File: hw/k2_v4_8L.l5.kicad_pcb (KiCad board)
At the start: 8 copper layers, 120 x 46 mm, 59 parts, among them J11 J_EC_HEADER, J12 J_12V_IN, J13 J_SWD, J2 SlimSAS_x8_SFF8654, J3 MCIO_4i_SFF1016, J4 MCIO_4i_SFF1016, J6 J_PWR_CTRL, J9 J_OOB_HEADER, U1 STM32G0B1CBT6, U2 DCDC_12V_3V3, U4 BAT54C, U5 OPTO_LTV356T, U6 DS320PR1601

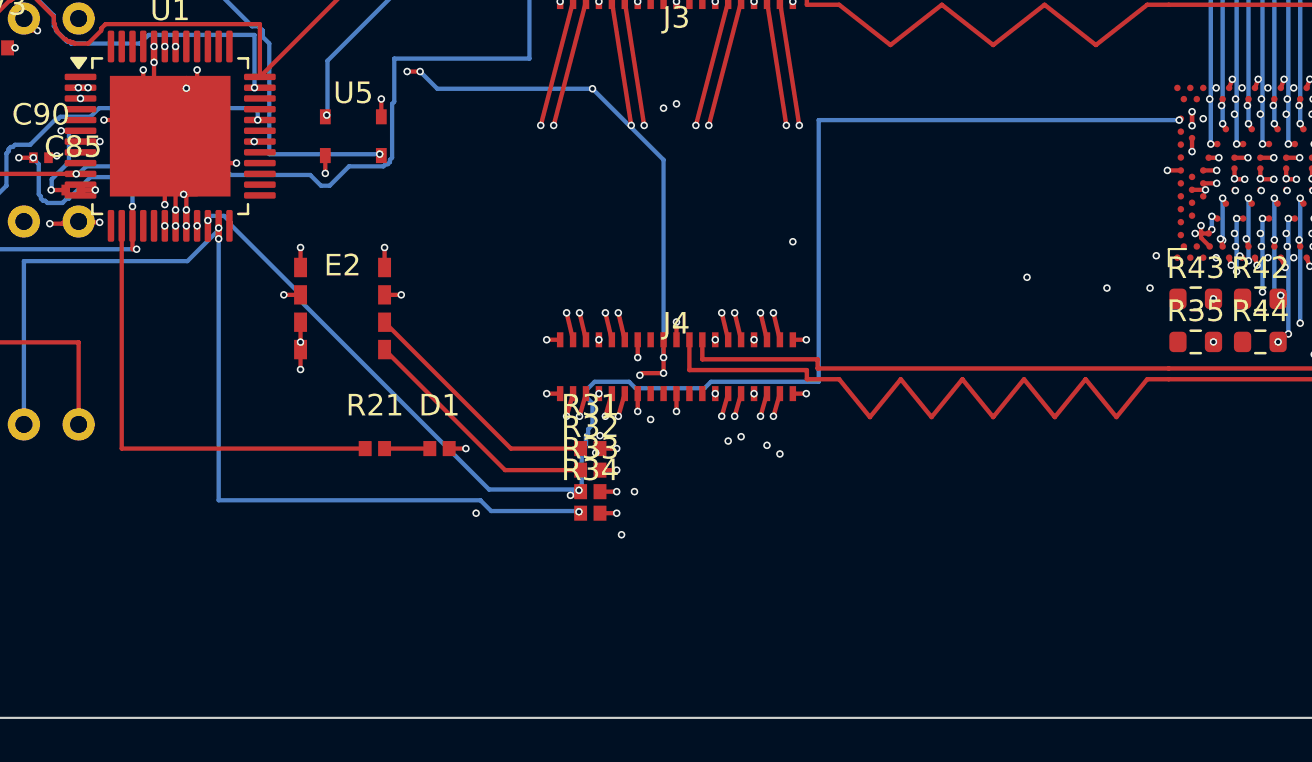
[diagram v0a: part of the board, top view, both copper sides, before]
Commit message: p4(k2): 收敛增量 7（L2 自裁）—— 跨层布线搜索加强（阶段 F3 修订）+ T-8 测量陷阱登记
- F3 修订：过孔搜索半径 1.5->2.5mm、角步 15->10 度；每端锚点 3->8；收尾连接器补 45+轴两段变体（口径/精确复核放行闸不变）。
- 实测：未连接 31 -> 29（+2 条）；违规 75 -> 75（类型集不变）；判定器 PASS5/FAIL5 集合未变；非 45 度 2051 未增。
- T-8（测量陷阱）：以无同名 .kicad_pro 的中间件为输入时，输出件缺 pro => kicad-cli drc 回退 KiCad 默认规则
  （min via 0.5 / track 0.2 / drill 0.3 / 板边 0.5），把板内既有 0.20/0.35 过孔与 0.16 PCIe 走线全判违规
  （本轮实测假象 1020 条）=> DRC 结论一律取「仓库路径 + 同名 pro」口径。
- 结构性结论：剩余 29 条 = no-legal-via-slot 14（U6 BGA 格内球无 F.Cu 逃逸通道）+ no-legal-path-on-bcu 15（J2 长距离段）
  => 续做须重解 U6 逃逸走廊（走廊 = L2，可自裁）或请监理裁定口径。
- 边界：未动 l4/设计源板/真源 yaml/criteria/SPEC rev-19..34 原件；未派 WORKER；临时仅 /tmp/opencode。
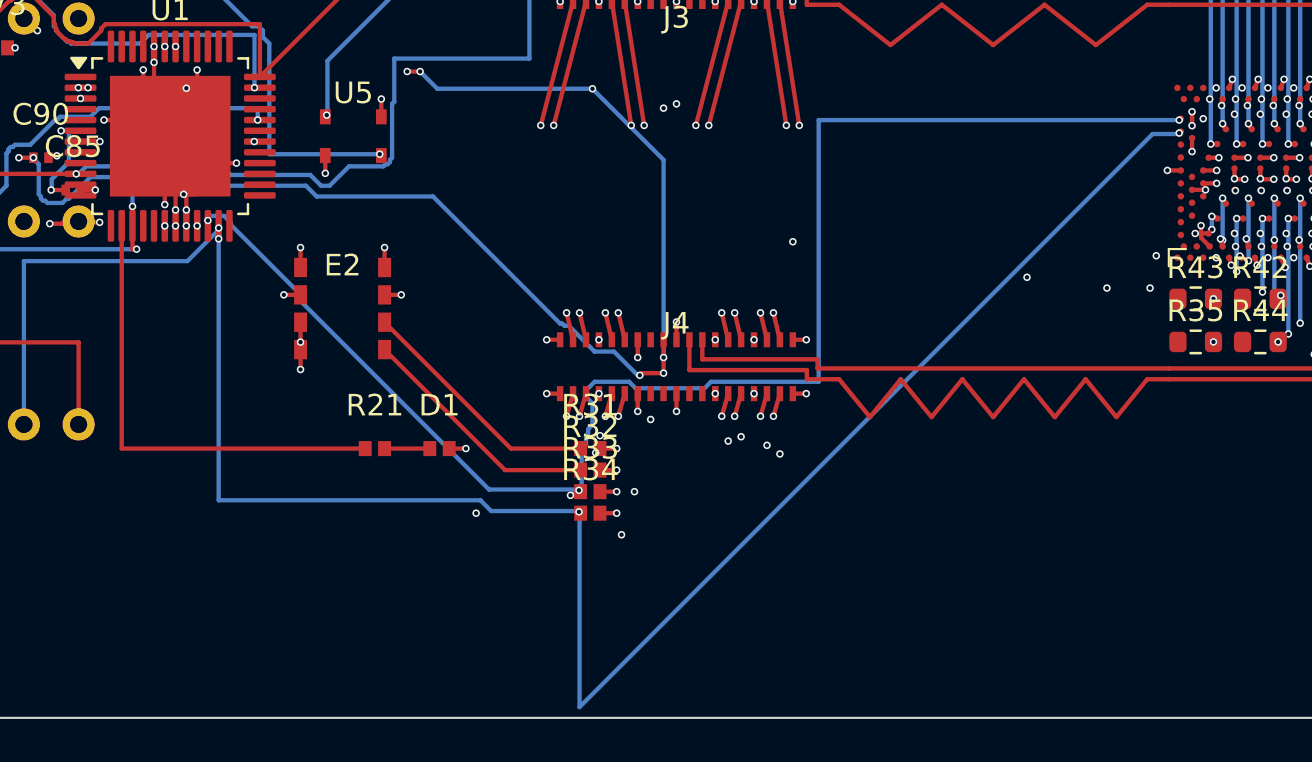
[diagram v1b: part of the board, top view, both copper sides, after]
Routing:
- net I2C2_SDA: track 47.2 -> 95.2 mm, vias 3 -> 4
- net P3V3_AUX: track 58.7 -> 86.1 mm
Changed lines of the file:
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@@
 	)
 	(segment
+		(start 42.3 54.3)
+		(end 42.8 54.8)
+		(width 0.2)
+		(layer "B.Cu")
+		(net "P3V3_AUX")
+	)
+	(segment
 		(start 58.9 53.1)
 		(end 58.9 62.275)
@@
 	)
 	(segment
+		(start 57.7 63.1)
+		(end 57.8 63.1)
+		(width 0.2)
+		(layer "B.Cu")
+		(net "P3V3_AUX")
+	)
+	(segment
+		(start 38.6 54.3)
+		(end 42.3 54.3)
+		(width 0.2)
+		(layer "B.Cu")
+		(net "P3V3_AUX")
+	)
+	(segment
 		(start 30.1 55)
 		(end 30.2 55)
@@
 	)
 	(segment
+		(start 34.2 53.9)
+		(end 38.2 53.9)
+		(width 0.2)
+		(layer "B.Cu")
+		(net "P3V3_AUX")
+	)
+	(segment
 		(start 26.5 57.2458)
 		(end 34.441 57.2458)
@@
 	)
 	(segment
+		(start 48.2 54.8)
+		(end 54.1 60.7)
+		(width 0.2)
+		(layer "B.Cu")
+		(net "P3V3_AUX")
+	)
+	(segment
+		(start 38.2 53.9)
+		(end 38.6 54.3)
+		(width 0.2)
+		(layer "B.Cu")
+		(net "P3V3_AUX")
+	)
+	(segment
 		(start 30.2 55)
 		(end 30.3 55.1)
@@
 	)
 	(segment
+		(start 54.5 60.8)
+		(end 55.7 62)
+		(width 0.2)
+		(layer "B.Cu")
+		(net "P3V3_AUX")
+	)
+	(segment
+		(start 54.1 60.7)
+		(end 54.2 60.7)
+		(width 0.2)
+		(layer "B.Cu")
+		(net "P3V3_AUX")
+	)
+	(segment
+		(start 42.8 54.8)
+		(end 48.2 54.8)
+		(width 0.2)
+		(layer "B.Cu")
+		(net "P3V3_AUX")
+	)
+	(segment
+		(start 54.3 60.8)
+		(end 54.5 60.8)
+		(width 0.2)
+		(layer "B.Cu")
+		(net "P3V3_AUX")
+	)
+	(segment
+		(start 54.2 60.7)
+		(end 54.3 60.8)
+		(width 0.2)
+		(layer "B.Cu")
+		(net "P3V3_AUX")
+	)
+	(segment
 		(start 29.9 54.7)
 		(end 30 54.8)
@@
 	)
 	(segment
+		(start 56.6 62)
+		(end 57.7 63.1)
+		(width 0.2)
+		(layer "B.Cu")
+		(net "P3V3_AUX")
+	)
+	(segment
 		(start 30 54.8)
 		(end 30 54.9)
@@
 	)
 	(segment
+		(start 55.7 62)
+		(end 56.6 62)
+		(width 0.2)
+		(layer "B.Cu")
+		(net "P3V3_AUX")
+	)
+	(segment
 		(start 47.6 49)
 		(end 48.4 49.8)
@@
 	)
 	(segment
+		(start 82.91 51.79)
+		(end 82.8334 51.79)
+		(width 0.2)
+		(layer "F.Cu")
+		(net "I2C2_SDA")
+	)
+	(segment
 		(start 38.25 56.1625)
 		(end 38.25 56.7625)
@@
 		(net "I2C2_SDA")
 	)
+	(segment
+		(start 82.8334 51.79)
+		(end 82.8334 51.8543)
+		(width 0.2)
+		(layer "F.Cu")
+		(net "I2C2_SDA")
+	)
+	(via
+		(at 82.8334 51.8543)
+		(size 0.35)
+		(drill 0.2)
+		(layers "F.Cu" "B.Cu")
+		(net "I2C2_SDA")
+	)
 	(via
 		(at 38.25 56.7625)
@@
 	)
 	(segment
+		(start 82.8 51.9)
+		(end 81.6 51.9)
+		(width 0.2)
+		(layer "B.Cu")
+		(net "I2C2_SDA")
+	)
+	(segment
 		(start 38.25 68.9)
 		(end 38.25 56.7625)
 		(width 0.2)
 		(layer "B.Cu")
+		(net "I2C2_SDA")
+	)
+	(segment
+		(start 55 78.5)
+		(end 55 69.4)
+		(width 0.2)
+		(layer "B.Cu")
+		(net "I2C2_SDA")
+	)
+	(segment
+		(start 81.6 51.9)
+		(end 55 78.5)
+		(width 0.2)
+		(layer "B.Cu")

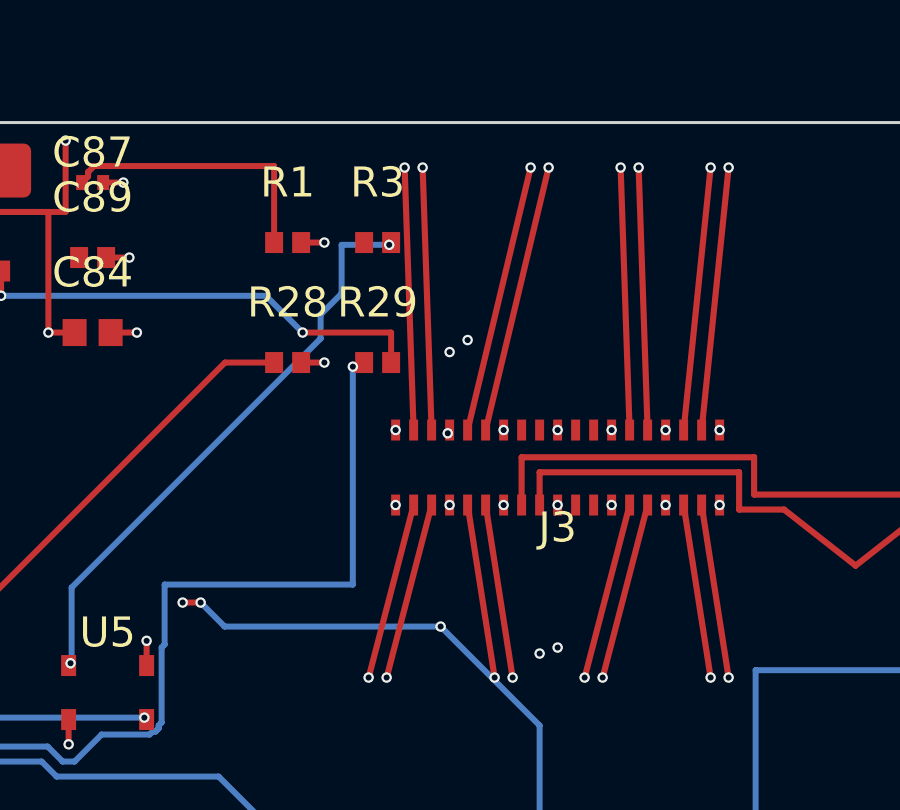
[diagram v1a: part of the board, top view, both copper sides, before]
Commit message: p4(k2): 收敛增量 8（L2 自裁）—— 阶段 F3 逃逸加强（盘中孔 VIP 兜底 + F.Cu A* 多腿逃逸）+ T-9/G-1 登记
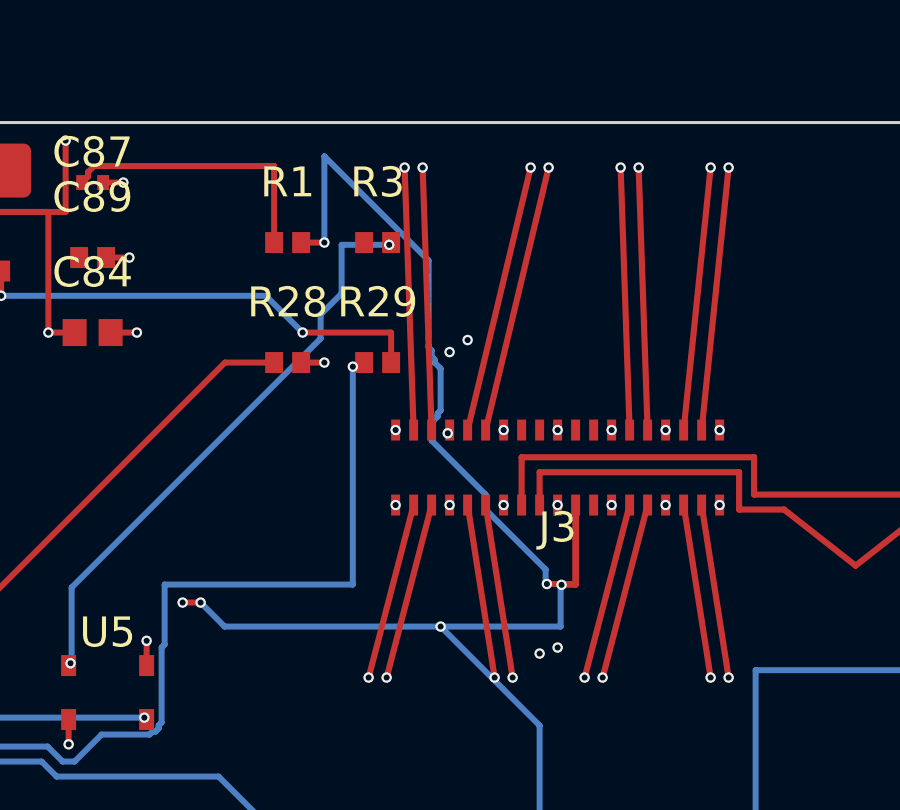
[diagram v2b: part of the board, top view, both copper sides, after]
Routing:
- net P3V3_AUX: track 86.1 -> 118.6 mm, vias 12 -> 14
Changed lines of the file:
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@@
+	)
+	(segment
+		(start 60.1 48.3811)
+		(end 59.1423 48.3811)
+		(width 0.2)
+		(layer "F.Cu")
+		(net "P3V3_AUX")
 	)
 	(segment
@@
 	)
 	(segment
+		(start 60.1 45.8)
+		(end 60.1 48.409)
+		(width 0.2)
+		(layer "F.Cu")
+		(net "P3V3_AUX")
+	)
+	(segment
 		(start 57.9 63)
 		(end 58.9 63)
@@
 	)
 	(segment
+		(start 60.1 45.8)
+		(end 60.1 48.3811)
+		(width 0.2)
+		(layer "F.Cu")
+		(net "P3V3_AUX")
+	)
+	(segment
+		(start 60.1 48.409)
+		(end 59.6311 48.409)
+		(width 0.2)
+		(layer "F.Cu")
+		(net "P3V3_AUX")
+	)
+	(segment
 		(start 31.75 61.57)
 		(end 31.75 65.38)
@@
 	)
 	(via
+		(at 59.6311 48.409)
+		(size 0.35)
+		(drill 0.2)
+		(layers "F.Cu" "B.Cu")
+		(net "P3V3_AUX")
+	)
+	(via
 		(at 26.5 61.57)
 		(size 0.35)
@@
 	(via
 		(at 47 49)
+		(size 0.35)
+		(drill 0.2)
+		(layers "F.Cu" "B.Cu")
+		(net "P3V3_AUX")
+	)
+	(via
+		(at 59.1423 48.3811)
 		(size 0.35)
 		(drill 0.2)
@@
 	)
 	(segment
+		(start 59.6 48.4)
+		(end 59.6 49.8)
+		(width 0.2)
+		(layer "B.Cu")
+		(net "P3V3_AUX")
+	)
+	(segment
 		(start 58.9 53.1)
 		(end 58.9 62.275)
@@
 	)
 	(segment
+		(start 55.2 40.5)
+		(end 55.2 37.6)
+		(width 0.2)
+		(layer "B.Cu")
+		(net "P3V3_AUX")
+	)
+	(segment
 		(start 30.3 55.1)
 		(end 31 55.1)
@@
 	)
 	(segment
+		(start 57.1 45.4)
+		(end 55.3 43.6)
+		(width 0.2)
+		(layer "B.Cu")
+		(net "P3V3_AUX")
+	)
+	(segment
+		(start 55.6 41.2)
+		(end 55.4 41)
+		(width 0.2)
+		(layer "B.Cu")
+		(net "P3V3_AUX")
+	)
+	(segment
+		(start 55.3 43)
+		(end 55.5 42.8)
+		(width 0.2)
+		(layer "B.Cu")
+		(net "P3V3_AUX")
+	)
+	(segment
+		(start 57.1 45.9)
+		(end 57.1 45.4)
+		(width 0.2)
+		(layer "B.Cu")
+		(net "P3V3_AUX")
+	)
+	(segment
 		(start 34.25 53.9)
 		(end 34.25 55.2625)
@@
 	)
 	(segment
+		(start 55.5 42.8)
+		(end 55.5 42.7)
+		(width 0.2)
+		(layer "B.Cu")
+		(net "P3V3_AUX")
+	)
+	(segment
 		(start 48.2 54.8)
 		(end 54.1 60.7)
@@
 	)
 	(segment
+		(start 55.4 41)
+		(end 55.4 40.9)
+		(width 0.2)
+		(layer "B.Cu")
+		(net "P3V3_AUX")
+	)
+	(segment
+		(start 55.2 37.6)
+		(end 51.725 34.125)
+		(width 0.2)
+		(layer "B.Cu")
+		(net "P3V3_AUX")
+	)
+	(segment
 		(start 30.2 55)
 		(end 30.3 55.1)
@@
 	)
 	(segment
+		(start 51.725 34.125)
+		(end 51.725 37)
+		(width 0.2)
+		(layer "B.Cu")
+		(net "P3V3_AUX")
+	)
+	(segment
 		(start 54.5 60.8)
 		(end 55.7 62)
@@
 	)
 	(segment
+		(start 59.1 48.4)
+		(end 59.1 47.9)
+		(width 0.2)
+		(layer "B.Cu")
+		(net "P3V3_AUX")
+	)
+	(segment
+		(start 55.4 40.9)
+		(end 55.3 40.8)
+		(width 0.2)
+		(layer "B.Cu")
+		(net "P3V3_AUX")
+	)
+	(segment
 		(start 54.3 60.8)
 		(end 54.5 60.8)
@@
 	)
 	(segment
+		(start 55.6 42.6)
+		(end 55.6 41.2)
+		(width 0.2)
+		(layer "B.Cu")
+		(net "P3V3_AUX")
+	)
+	(segment
 		(start 29.9 54.7)
 		(end 30 54.8)
@@
 	)
 	(segment
+		(start 55.3 40.6)
+		(end 55.2 40.5)
+		(width 0.2)
+		(layer "B.Cu")
+		(net "P3V3_AUX")
+	)
+	(segment
 		(start 56.6 62)
 		(end 57.7 63.1)
@@
 		(width 0.2)
 		(layer "B.Cu")
+		(net "P3V3_AUX")
+	)
+	(segment
+		(start 59.6 49.8)
+		(end 55.6 49.8)
+		(width 0.2)
+		(layer "B.Cu")
+		(net "P3V3_AUX")
+	)
+	(segment
+		(start 55.5 42.7)
+		(end 55.6 42.6)
+		(width 0.2)
+		(layer "B.Cu")
+		(net "P3V3_AUX")
+	)
+	(segment
+		(start 55.3 40.8)
+		(end 55.3 40.6)
+		(width 0.2)
+		(layer "B.Cu")
+		(net "P3V3_AUX")
+	)
+	(segment
+		(start 59.1 47.9)
+		(end 57.1 45.9)
+		(width 0.2)
+		(layer "B.Cu")
+		(net "P3V3_AUX")
+	)
+	(segment
+		(start 55.3 43.6)
+		(end 55.3 43)
+		(width 0.2)
+		(layer "B.Cu")

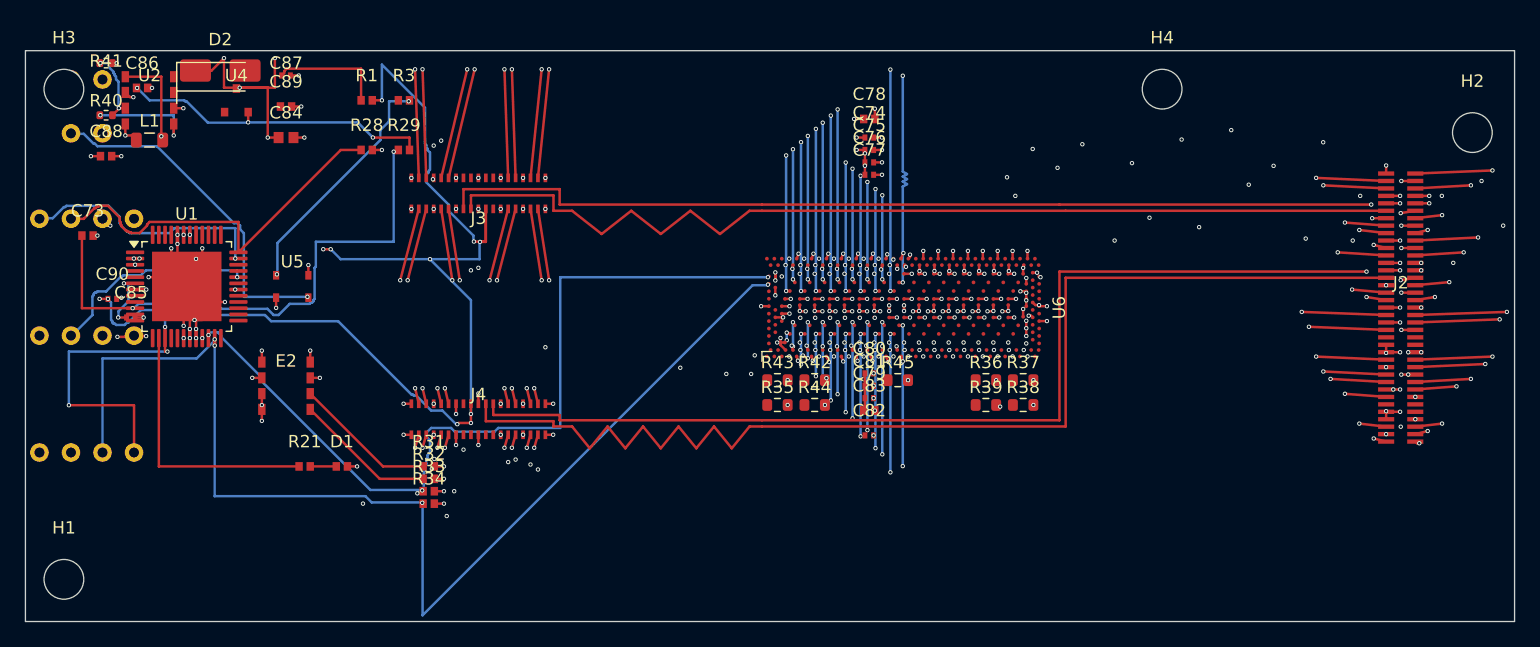
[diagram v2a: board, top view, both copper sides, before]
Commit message: p4(k2): 收敛增量 9（L2 自裁）—— 阶段 G：低速/边带 F.Cu→In2 盲孔 + In2 通道布线（span 感知判定 + 候选多样化 + F.Cu 直连优先）+ T-10/T-11/T-12 登记
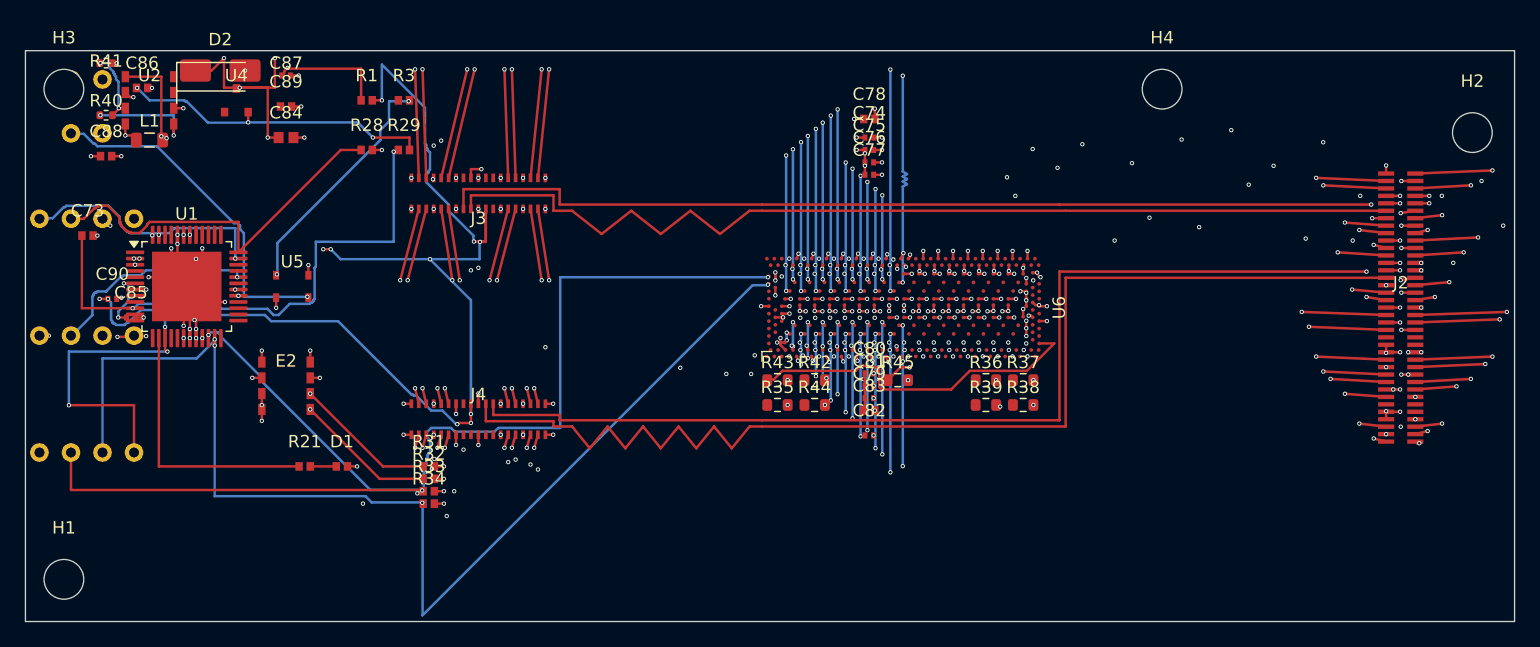
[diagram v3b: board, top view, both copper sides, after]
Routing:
- net PERSTA#: track 9.27 -> 51.5 mm, vias 0 -> 2
- net UART_TX: track 0.00 -> 40.8 mm, vias 0 -> 2
- net I2C1_SDA: track 11.4 -> 43.1 mm, vias 0 -> 2
- net I2C2_SCL: track 69.6 -> 100.9 mm
- net DS320_STRAP_A_ADDR1_15-8: track 0.00 -> 27.9 mm
- net I2C1_SCL: track 11.5 -> 34.7 mm, vias 0 -> 2
- net DS320_STRAP_B_ADDR1_15-8: track 0.00 -> 17.7 mm, vias 0 -> 2
- net SW_U2: track 7.71 -> 20.0 mm, vias 1 -> 3
